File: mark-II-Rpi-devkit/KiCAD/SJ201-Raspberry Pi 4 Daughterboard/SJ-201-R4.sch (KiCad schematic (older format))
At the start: 7 parts

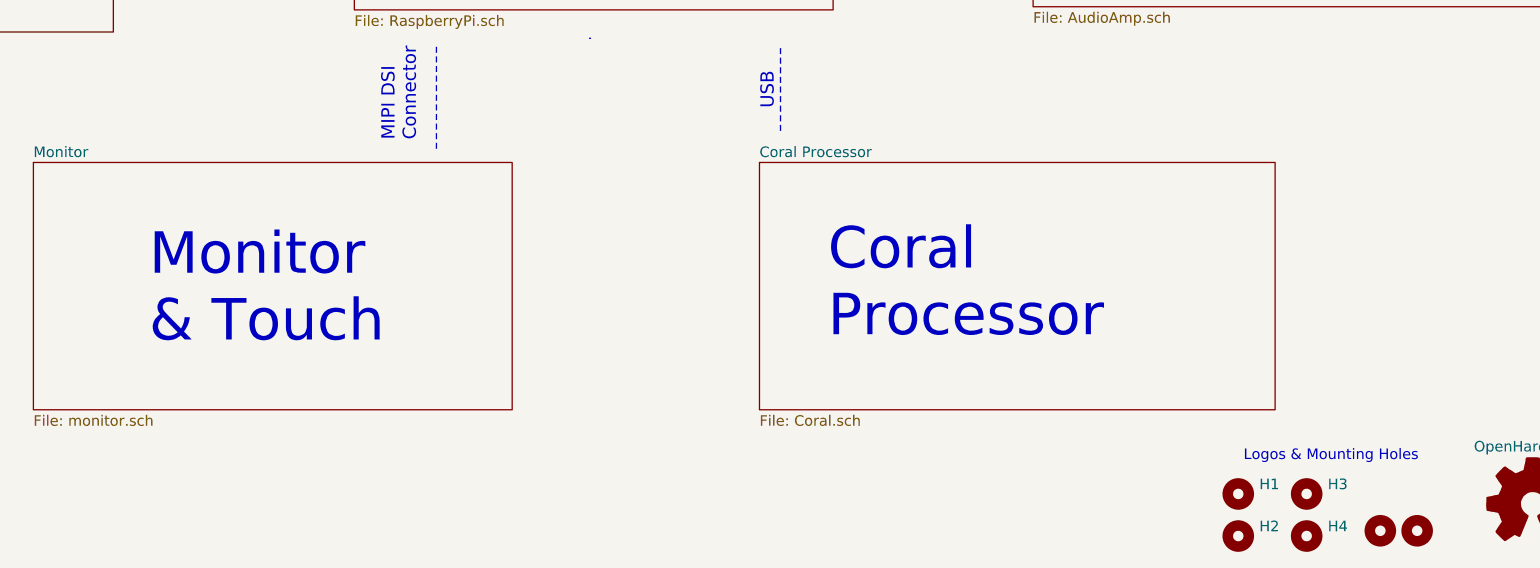
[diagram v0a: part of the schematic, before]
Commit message: Rev4 Update - fix some wiring, export for printing Rev 4
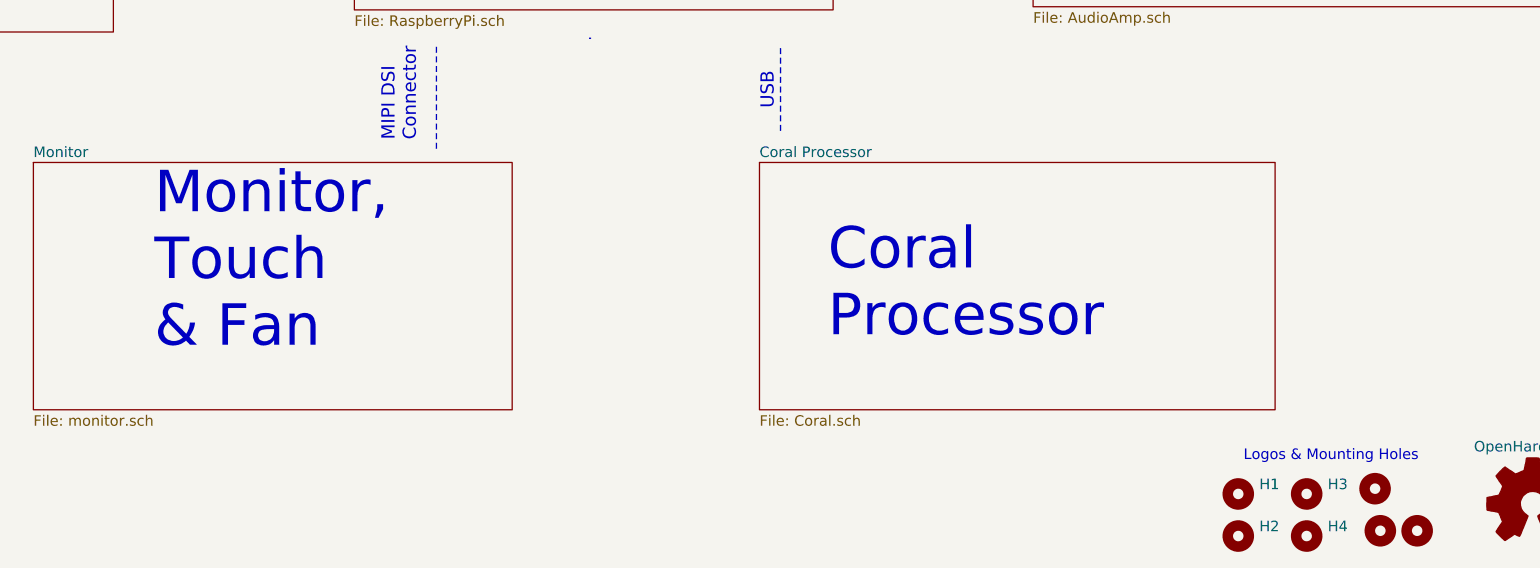
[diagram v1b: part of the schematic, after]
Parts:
- added H6: MountingHole, libraries:simon-jestor-logo, symbol Mechanical:MountingHole
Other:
- note added: "Monitor, \nTouch\n& Fan"
- note removed: "Monitor\n& Touch"
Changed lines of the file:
@@
 Sheet 1 7
 Title "SJ-201+"
-Date "2020-11-18"
-Rev "rev4 - 0.01"
+Date "2020-11-22"
+Rev "Rev4 - 0.03"
 Comp "Mycroft"
-Comment1 "SJ201 r4.01"
+Comment1 "SJ-201-R4"
 Comment2 ""
 Comment3 ""
@@
 Text Notes 1400 3625 0    197  ~ 0
 Power
-Text Notes 3300 5775 0    197  ~ 0
-Monitor\n& Touch
+Text Notes 3325 5800 0    197  ~ 0
+Monitor, \nTouch\n& Fan
 Wire Notes Line
 	3380 3540 4060 3540
@@
 Text Notes 5625 2625 2    63   ~ 0
 I2S
+$Comp
+L Mechanical:MountingHole H6
+U 1 1 60926A26
+P 9125 6450
+F 0 "H6" H 9225 6496 50  0001 L CNN
+F 1 "MountingHole" H 9225 6405 50  0001 L CNN
+F 2 "libraries:simon-jestor-logo" H 9125 6450 50  0001 C CNN
+F 3 "~" H 9125 6450 50  0001 C CNN
+F 4 "DNP" H 9125 6450 50  0001 C CNN "MPN"
+	1    9125 6450
+	1    0    0    -1
+$EndComp
 $EndSCHEMATC
